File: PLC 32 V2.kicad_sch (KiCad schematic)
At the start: 9 parts, among them J2 Screw_Terminal_01x05, J3 Screw_Terminal_01x05, J5 Screw_Terminal_01x10, J6 Screw_Terminal_01x02, J7 MODULO RTC, J8 Screw_Terminal_01x02, U18 ESP32-WROOM-32D, U30 74HC373

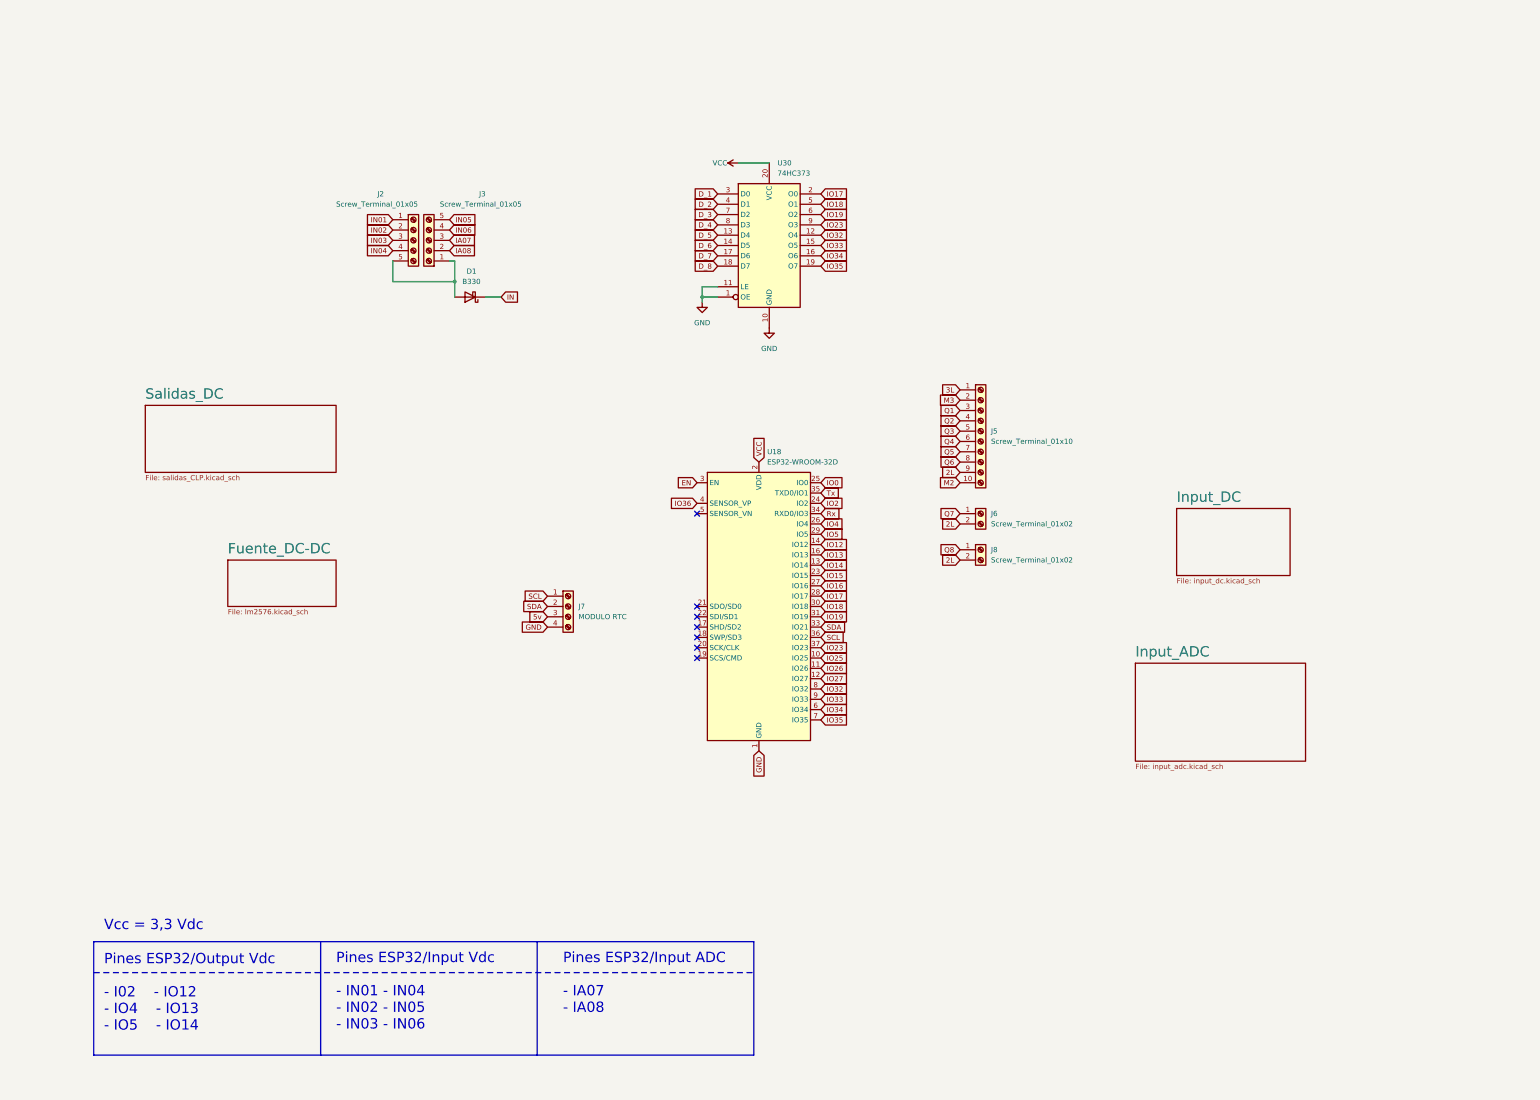
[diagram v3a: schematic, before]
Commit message: Documentación pines esp32
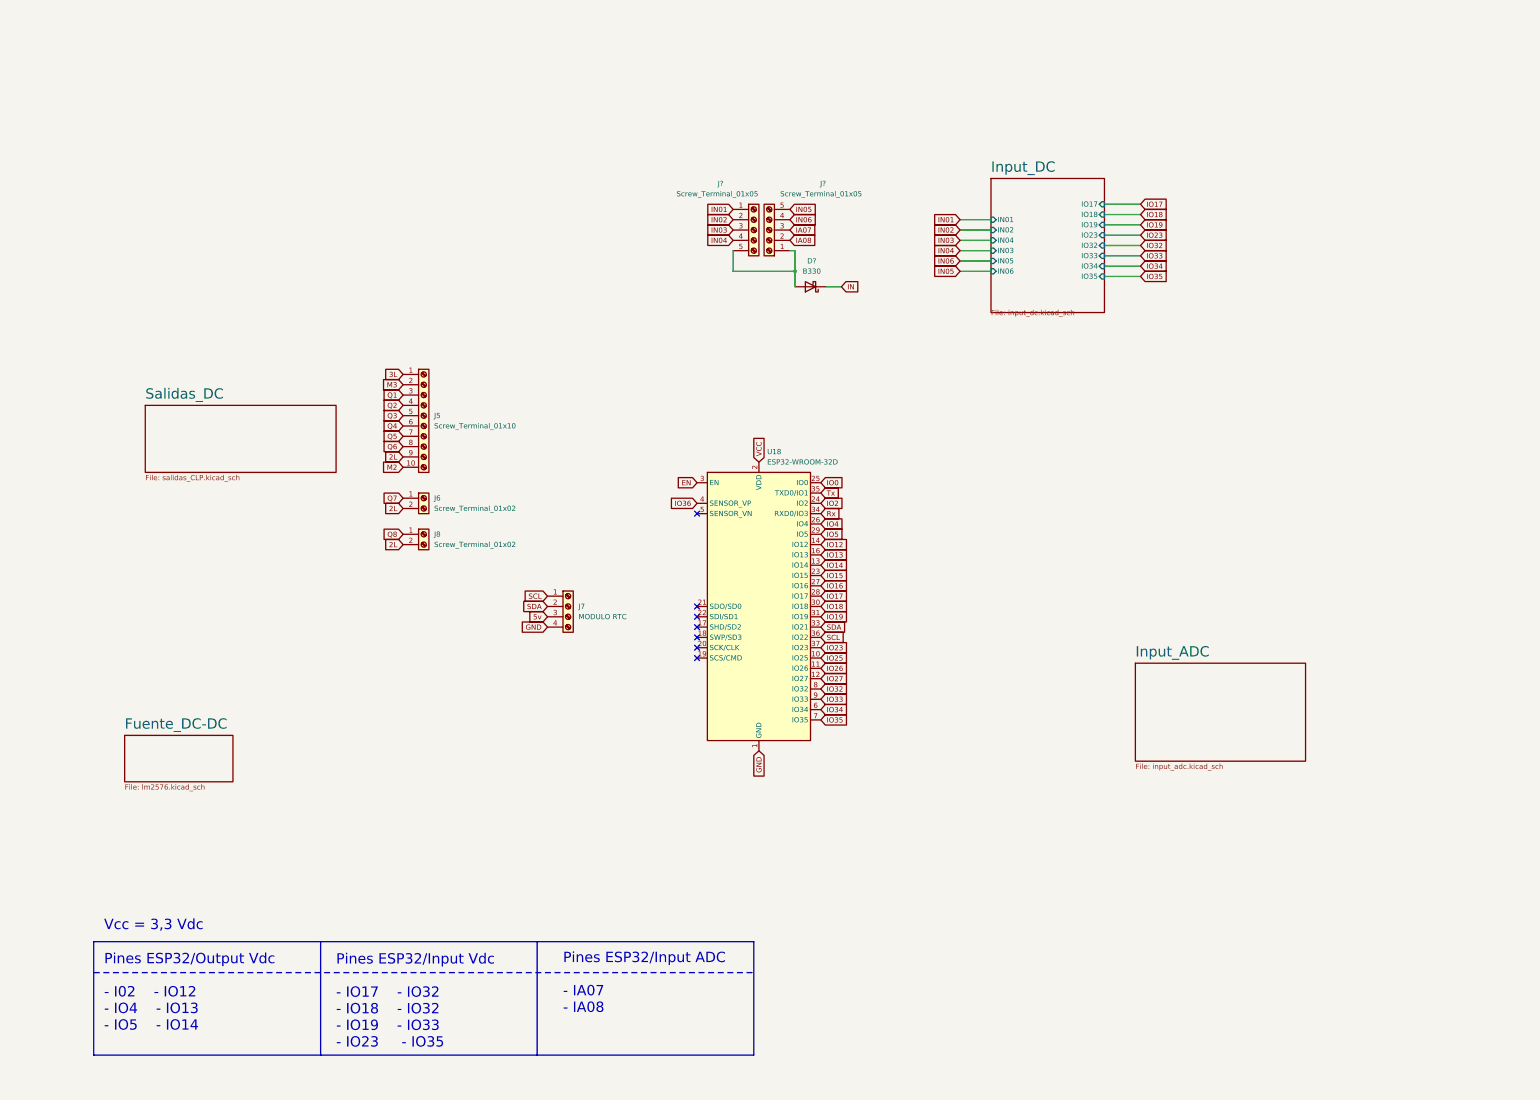
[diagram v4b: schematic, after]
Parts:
- removed D1: B330, Diode_SMD:D_0402_1005Metric, symbol Diode:B330
- removed J2, J3: Screw_Terminal_01x05, TerminalBlock:TerminalBlock_bornier-5_P5.08mm, symbol Connector:Screw_Terminal_01x05
- removed U30: 74HC373, Package_SO:SSOP-20_4.4x6.5mm_P0.65mm, symbol 74xx:74HC373
- added D?: B330, Diode_SMD:D_0402_1005Metric, symbol Diode:B330
- added J? (x2): Screw_Terminal_01x05, TerminalBlock:TerminalBlock_bornier-5_P5.08mm, symbol Connector:Screw_Terminal_01x05
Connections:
- net IA07: now also J?.3 (Pin_3)
- net IA08: now also J?.2 (Pin_2)
- net IN: now also D?.1 (K)
- net IN01: now also J?.1 (Pin_1)
- net IN02: now also J?.2 (Pin_2)
- net IN03: now also J?.3 (Pin_3)
- net IN04: now also J?.4 (Pin_4)
- net IN05: now also J?.5 (Pin_5)
- net IN06: now also J?.4 (Pin_4)
- new net: D?.2 (A), J?.1 (Pin_1), J?.5 (Pin_5)
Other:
- sheet Input_DC ports: added IN01, IN02, IN03, IN04, IN05, IN06, IO17, IO18, IO19, IO23, IO32, IO33, IO34, IO35; removed none
- note added: "Pines ESP32/Input Vdc - IO17 - IO32 - IO18 - IO32 - IO19 - IO33 - IO23 - IO35"
- note removed: "Pines ESP32/Input Vdc - IN01 - IN04 - IN02 - IN05 - IN03 - IN06"
- moved on the sheet: J5, J6, J8

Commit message: update esq raiz
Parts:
- J5: value Screw_Terminal_01x10 -> Salidas Q1 - Q5
- J6: value Screw_Terminal_01x02 -> Salida Q7
- J8: value Screw_Terminal_01x02 -> Salida Q8
- J?: value Screw_Terminal_01x05 -> Input_1
- J?: value Screw_Terminal_01x05 -> Input_2
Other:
- sheet Fuente_DC-DC ports: added Vcc, gnd; removed none
- sheet Salidas_DC ports: added 2L, 3L, IO02, IO04, IO05, IO12, IO13, IO14, Q1, Q2, Q3, Q4, Q5, Q6; removed none
- note added: "Pines Módulo ESP32-WROOM"
- moved on the sheet: D?, J5, J6, J7, J8, J?, U18

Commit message: update esq raiz salidas
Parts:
- removed J6: Salida Q7, TerminalBlock:TerminalBlock_bornier-2_P5.08mm, symbol Connector:Screw_Terminal_01x02
- removed J8: Salida Q8, TerminalBlock:TerminalBlock_bornier-2_P5.08mm, symbol Connector:Screw_Terminal_01x02
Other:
- moved on the sheet: J5
